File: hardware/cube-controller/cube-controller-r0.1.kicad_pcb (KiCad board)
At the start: 4 copper layers, 50.4 x 44.7 mm, 85 parts, among them J2 Conn_01x20_Shielded, J3 Conn_01x20_Shielded, J4 Conn_02x05_Odd_Even, J5 USB_C_Receptacle_USB2.0, SW1 SW_Push, SW2 SW_Push, U1 LTC4367, U10 SN74AVC8T245PW, U11 SN74AVC8T245PW, U12 BMX160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

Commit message: Fix pin1 on SWD connector
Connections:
- J4 pad 1: gnd -> 3v3
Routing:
- net 3v3: track 50.4 -> 57.0 mm
- net 4v5: track 46.6 -> 47.8 mm
- net gnd: track 123.4 -> 122.4 mm
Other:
- board text added: "2019-10-14"
- board text removed: "2019-10-08"

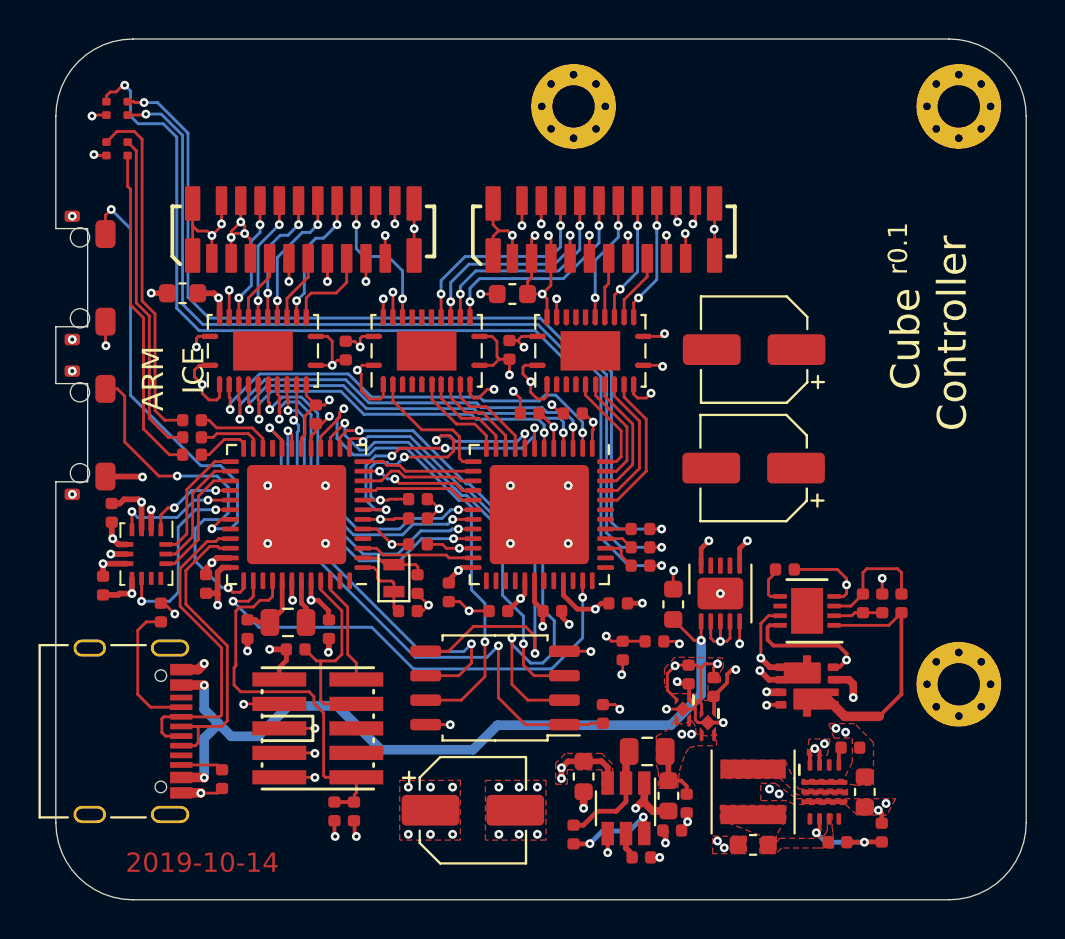
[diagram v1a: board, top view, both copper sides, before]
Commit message: Updated SKiDL to include orderable part numbers. Exported iBOM for r0.1 CubeController Added Gerbers for CubeController r0.1
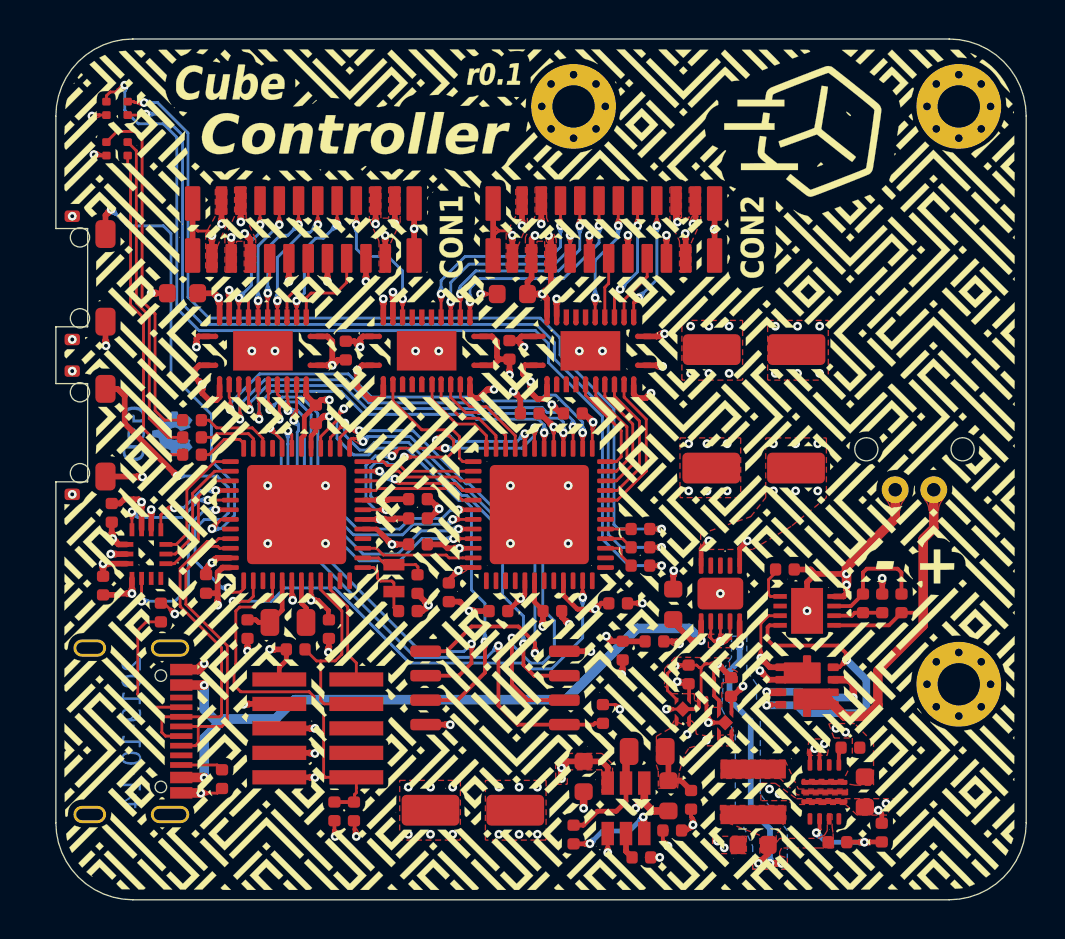
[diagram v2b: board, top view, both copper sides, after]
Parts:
- added G***: LOGO, gsd_logo_small, B.Cu at (141.2, 102.0)
- added G***: LOGO, oshw_small, B.Cu at (143.2, 102.0)
- added G***: LOGO, artwork_controller, F.Cu at (162.2, 103.8)
- added J1: Conn_01x02, gkl_conn:SB02B-PASK-2, F.Cu at (181.7, 104.9)
- moved C6 0.90 mm to (172.2, 115.1)
- moved U5 0.90 mm to (171.9, 117.0)
- moved R9 0.30 mm to (170.1, 121.0)
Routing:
- net 4v5: track 47.8 -> 124.2 mm, vias 29 -> 41
- net gnd: track 122.4 -> 148.2 mm, vias 90 -> 104
- net 4v5_in: track 1.16 -> 15.4 mm, vias 1 -> 4
- net pp_batt_prot: track 7.98 -> 19.4 mm
- net N$2: track 7.66 -> 16.0 mm
- net pp_batt: track 15.4 -> 23.3 mm
- net N$1: track 2.58 -> 7.21 mm
- net 5v0_usb: track 46.4 -> 42.9 mm
- net 3v3: track 57.0 -> 58.5 mm
- net 2v5: track 25.5 -> 24.4 mm
- net 1v2: track 27.8 -> 28.6 mm
- net ice_led_g: track 47.6 -> 47.0 mm
- net ice_led_r: track 51.1 -> 50.5 mm
- net N$31: track 25.2 -> 25.8 mm
- net N$42: track 18.6 -> 18.1 mm
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- added copper zone on B.Cu, net 4v5_in
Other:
- board text removed: "ARM"
- board text removed: "Controller"
- board text removed: "Cube"
- board text removed: "ICE"
- board text removed: "r0.1"
